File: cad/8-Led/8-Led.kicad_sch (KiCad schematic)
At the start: 21 parts, among them J1 Screw_Terminal_01x02

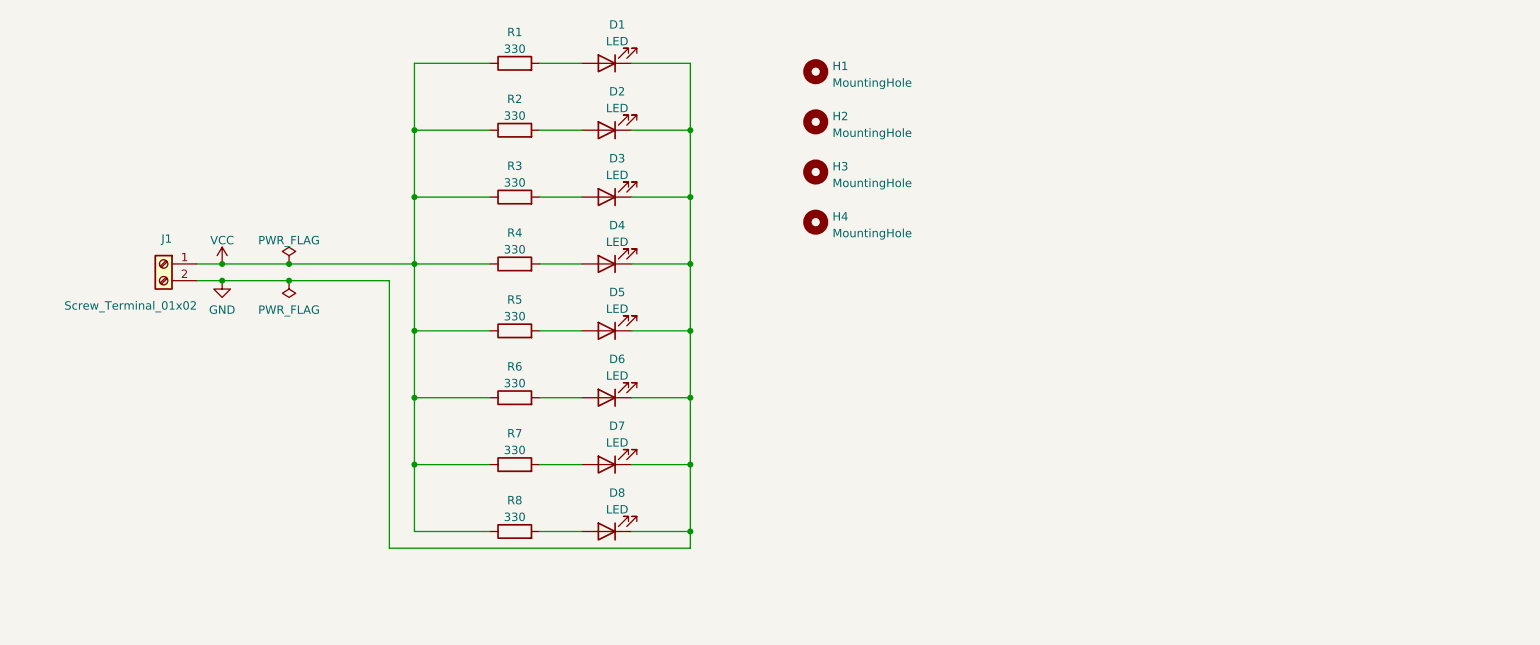
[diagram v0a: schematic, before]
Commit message: learn add lines in kicad for 8Led
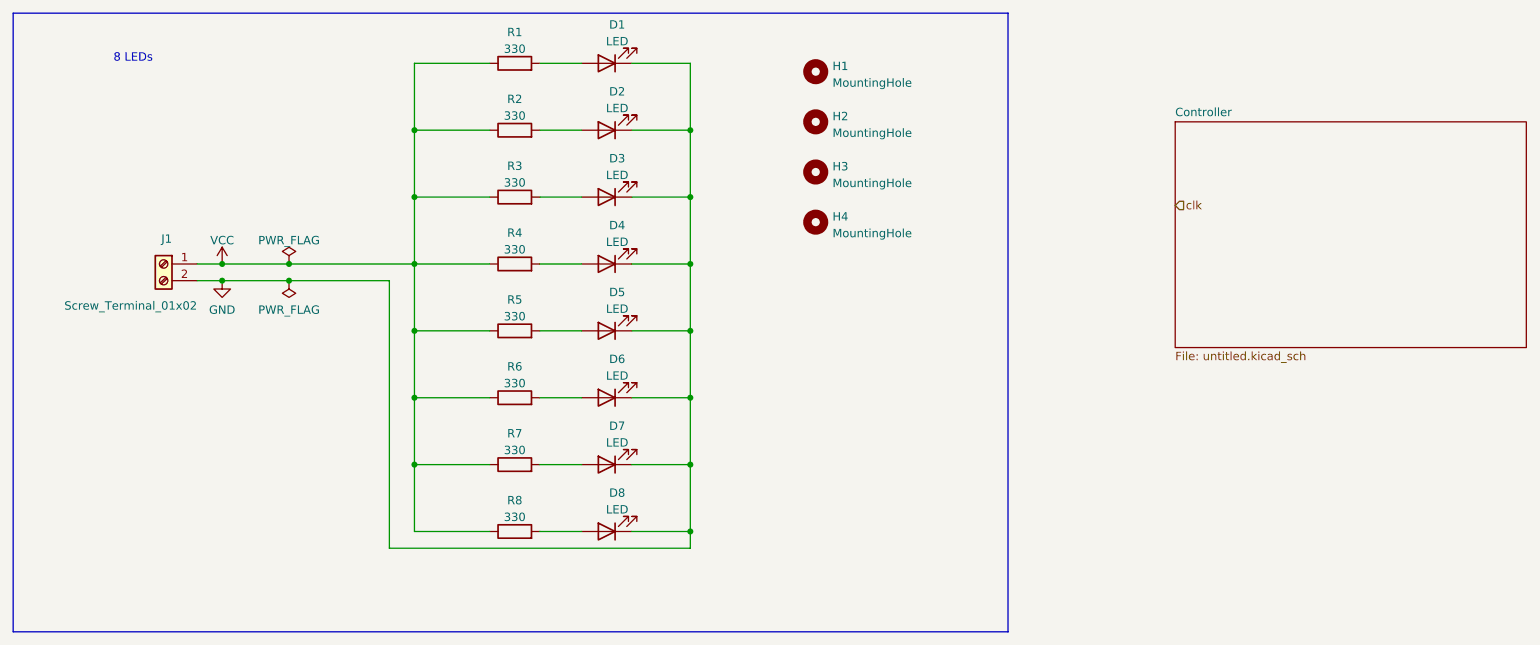
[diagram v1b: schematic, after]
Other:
- added sheet Controller (untitled.kicad_sch)
- note added: "8 LEDs"
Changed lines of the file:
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@@
+    (stroke (width 0) (type default) (color 0 0 0 0))
+  )
+  (polyline (pts (xy 179.07 20.32) (xy 179.07 114.3))
     (stroke (width 0) (type default) (color 0 0 0 0))
   )
@@
     (stroke (width 0) (type default) (color 0 0 0 0))
   )
+  (polyline (pts (xy 27.94 20.32) (xy 179.07 20.32))
+    (stroke (width 0) (type default) (color 0 0 0 0))
+  )
   (wire (pts (xy 88.9 38.1) (xy 100.33 38.1))
     (stroke (width 0) (type default) (color 0 0 0 0))
@@
     (stroke (width 0) (type default) (color 0 0 0 0))
   )
+  (polyline (pts (xy 179.07 114.3) (xy 27.94 114.3))
+    (stroke (width 0) (type default) (color 0 0 0 0))
+  )
+  (polyline (pts (xy 27.94 20.32) (xy 27.94 114.3))
+    (stroke (width 0) (type default) (color 0 0 0 0))
+  )
   (wire (pts (xy 107.95 78.74) (xy 114.3 78.74))
     (stroke (width 0) (type default) (color 0 0 0 0))
@@
   (wire (pts (xy 88.9 58.42) (xy 100.33 58.42))
     (stroke (width 0) (type default) (color 0 0 0 0))
+  )
+  (text "8 LEDs" (at 43.18 27.94 0)
+    (effects (font (size 1.27 1.27)) (justify left bottom))
+  )
+  (hierarchical_label "clk" (shape input) (at 204.47 49.53 0)
+    (effects (font (size 1.27 1.27)) (justify left))
   )
   (symbol (lib_id "Device:LED") (at 118.11 27.94 180) (unit 1)
@@
     (pin "2")
   )
+  (sheet (at 204.47 36.83) (size 53.34 34.29) (fields_autoplaced)
+    (stroke (width 0.1524) (type solid) (color 0 0 0 0))
+    (fill (color 0 0 0 0.0000))
+    (property "Sheet name" "Controller" (id 0) (at 204.47 36.1184 0)
+      (effects (font (size 1.27 1.27)) (justify left bottom))
+    )
+    (property "Sheet file" "untitled.kicad_sch" (id 1) (at 204.47 71.7046 0)
+      (effects (font (size 1.27 1.27)) (justify left top))
+    )
+  )
   (sheet_instances
     (path "/" (page "1"))
+    (path "/fadefa33-8e30-44c4-97be-46ad588ab9fb" (page "2"))
   )
   (symbol_instances
